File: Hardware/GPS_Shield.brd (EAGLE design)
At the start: 59.7 x 53.3 mm, 52 parts, among them J1 ARDUINO_R3_SHIELD, J2 USD_CONNECTOR, U1 APK2112-3.3V, U2 GP3906-TLP, U3 TXB0108

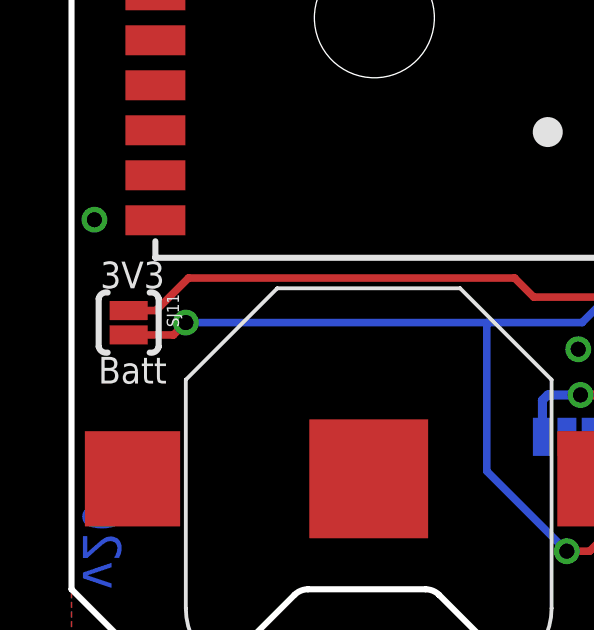
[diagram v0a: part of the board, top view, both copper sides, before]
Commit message: Default SJ11 to open.
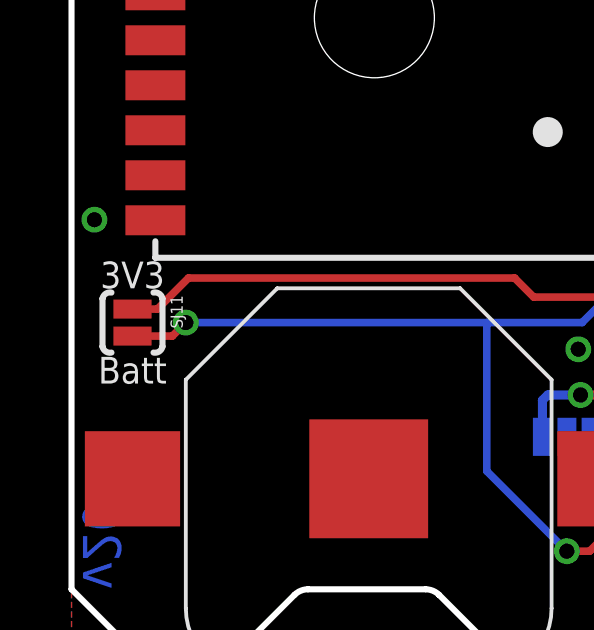
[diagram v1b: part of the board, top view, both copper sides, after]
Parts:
- SJ11: device SparkFun-Passives:PAD-JUMPER-2-NC_BY_PASTE_YES_SILK -> SparkFun-Passives:PAD-JUMPER-2-NO_YES_SILK
- moved SJ11 0.13 mm to (2.03, 11.4)
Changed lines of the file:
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@@
 <layer number="29" name="tStop" color="7" fill="3" visible="no" active="yes"/>
 <layer number="30" name="bStop" color="7" fill="6" visible="no" active="yes"/>
-<layer number="31" name="tCream" color="7" fill="4" visible="no" active="yes"/>
+<layer number="31" name="tCream" color="7" fill="4" visible="yes" active="yes"/>
 <layer number="32" name="bCream" color="7" fill="5" visible="no" active="yes"/>
 <layer number="33" name="tFinish" color="6" fill="3" visible="no" active="yes"/>
@@
 <attribute name="PROD_ID" value="CONN-08438" x="21.59" y="15.24" size="1.778" layer="27" font="vector" ratio="15" rot="R90" display="off"/>
 </element>
-<element name="SJ11" library="SparkFun-Passives" package="PAD-JUMPER-2-NC_BY_PASTE_YES_SILK" value="VBAT-3.3V" x="1.905" y="11.43" rot="R270"/>
+<element name="SJ11" library="SparkFun-Passives" package="PAD-JUMPER-2-NO_YES_SILK" value="VBAT-3.3V" x="2.032" y="11.43" rot="R270"/>
 </elements>
 <signals>
@@
 <wire x1="21.59" y1="5.08" x2="19.812" y2="6.858" width="0.3048" layer="16"/>
 <wire x1="17.995" y1="35.98" x2="19.265" y2="34.71" width="0.2032" layer="1"/>
-<contactref element="SJ11" pad="1"/>
 <wire x1="19.05" y1="12.28" x2="15.406" y2="12.28" width="0.254" layer="1"/>
 <wire x1="15.406" y1="12.28" x2="14.771" y2="12.915" width="0.254" layer="1"/>
-<wire x1="1.905" y1="11.8309" x2="2.8139" y2="11.8309" width="0.254" layer="1"/>
-<wire x1="2.8139" y1="11.8309" x2="3.898" y2="12.915" width="0.254" layer="1"/>
 <wire x1="3.898" y1="12.915" x2="14.771" y2="12.915" width="0.254" layer="1"/>
 <wire x1="19.812" y1="6.858" x2="19.812" y2="7.62" width="0.3048" layer="16"/>
@@
 <wire x1="19.812" y1="13.462" x2="21.59" y2="15.24" width="0.3048" layer="16"/>
 <wire x1="17.3228" y1="7.62" x2="19.812" y2="7.62" width="0.3048" layer="16"/>
+<contactref element="SJ11" pad="1"/>
+<wire x1="2.032" y1="11.88" x2="2.863" y2="11.88" width="0.254" layer="1"/>
+<wire x1="2.863" y1="11.88" x2="3.898" y2="12.915" width="0.254" layer="1"/>
 </signal>
 <signal name="5V">
@@
 <wire x1="21.59" y1="17.78" x2="19.05" y2="15.24" width="0.254" layer="16"/>
 <wire x1="19.05" y1="15.24" x2="19.05" y2="13.462" width="0.254" layer="16"/>
+<wire x1="3.36" y1="10.98" x2="3.81" y2="11.43" width="0.254" layer="1"/>
+<via x="3.81" y="11.43" extent="1-16" drill="0.508"/>
 <contactref element="SJ11" pad="2"/>
-<wire x1="1.905" y1="11.0173" x2="3.3973" y2="11.0173" width="0.254" layer="1"/>
-<wire x1="3.3973" y1="11.0173" x2="3.81" y2="11.43" width="0.254" layer="1"/>
-<via x="3.81" y="11.43" extent="1-16" drill="0.508"/>
+<wire x1="2.032" y1="10.98" x2="3.36" y2="10.98" width="0.254" layer="1"/>
 </signal>
 <signal name="CD">

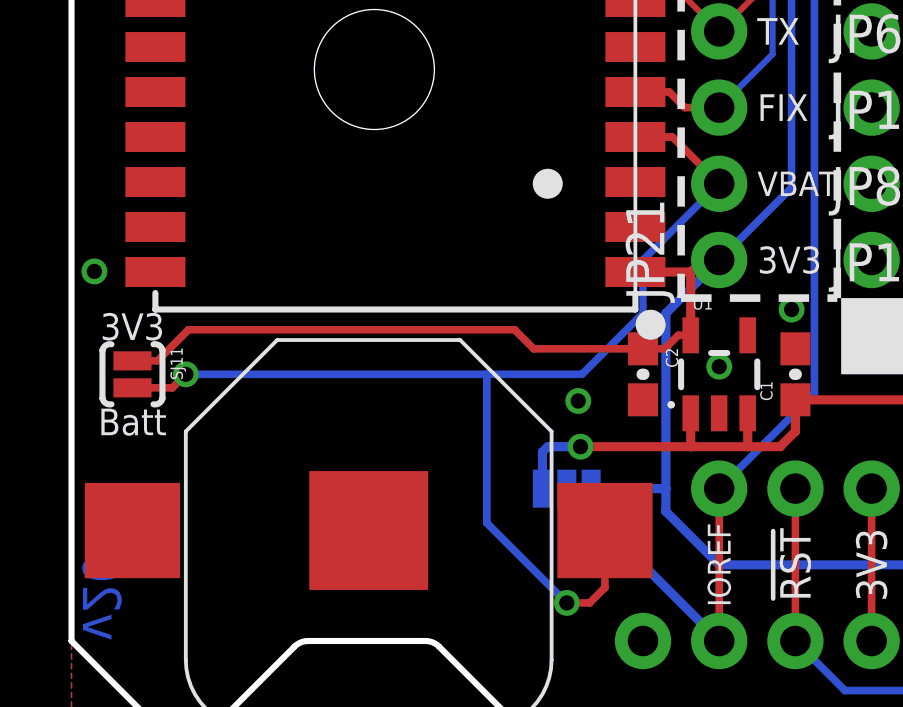
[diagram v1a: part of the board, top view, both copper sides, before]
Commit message: Adding note about battery required.
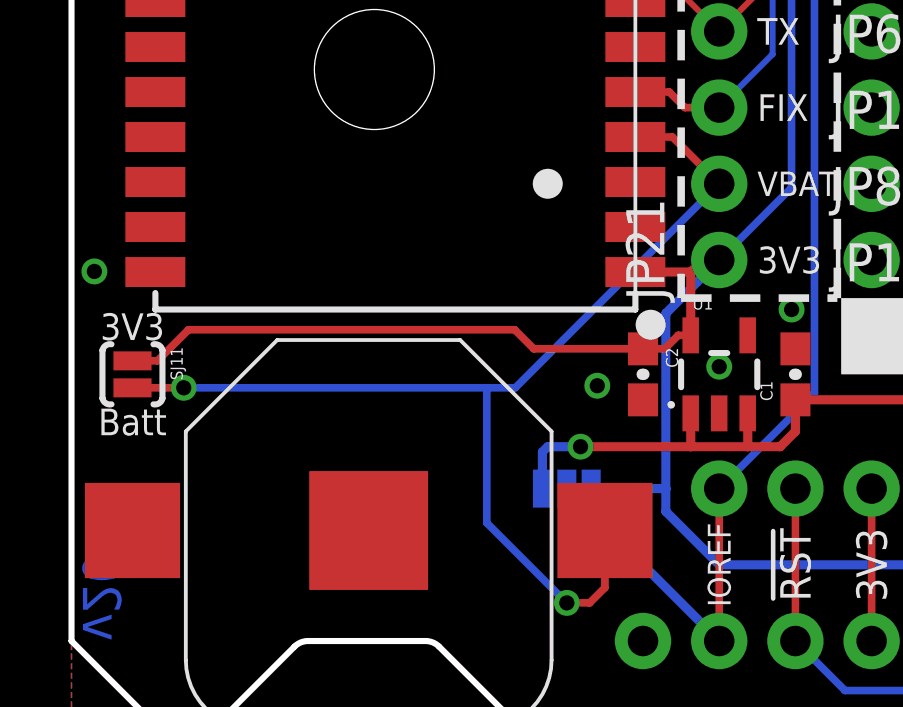
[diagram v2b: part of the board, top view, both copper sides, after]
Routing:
- net V_BATT: track 39.0 -> 37.5 mm
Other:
- board text added: "Battery supply required for operation!"
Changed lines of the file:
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@@
 <setting verticaltext="up"/>
 </settings>
-<grid distance="0.05" unitdist="inch" unit="inch" style="lines" multiple="1" display="yes" altdistance="0.0025" altunitdist="inch" altunit="inch"/>
+<grid distance="0.05" unitdist="inch" unit="inch" style="lines" multiple="1" display="yes" altdistance="0.005" altunitdist="inch" altunit="inch"/>
 <layers>
 <layer number="1" name="Top" color="4" fill="1" visible="yes" active="yes"/>
@@
 <layer number="29" name="tStop" color="7" fill="3" visible="no" active="yes"/>
 <layer number="30" name="bStop" color="7" fill="6" visible="no" active="yes"/>
-<layer number="31" name="tCream" color="7" fill="4" visible="yes" active="yes"/>
+<layer number="31" name="tCream" color="7" fill="4" visible="no" active="yes"/>
 <layer number="32" name="bCream" color="7" fill="5" visible="no" active="yes"/>
 <layer number="33" name="tFinish" color="6" fill="3" visible="no" active="yes"/>
@@
 <text x="53.6575" y="30.48" size="0.8128" layer="22" font="vector" ratio="15" rot="MR0" align="center-left">MISO</text>
 <text x="58.42" y="28.0035" size="0.8128" layer="22" font="vector" ratio="15" rot="MR270" align="top-center">MOSI</text>
+<text x="12.573" y="7.366" size="1.016" layer="22" font="vector" ratio="15" rot="MR0" align="top-left">Battery supply
+required for
+operation!</text>
 </plain>
 <attributes>
@@
 <via x="19.05" y="37.084" extent="1-16" drill="0.508"/>
 <via x="21.59" y="11.684" extent="1-16" drill="0.508"/>
-<via x="16.891" y="10.541" extent="1-16" drill="0.508"/>
+<via x="17.526" y="11.049" extent="1-16" drill="0.508"/>
 <via x="24.003" y="13.589" extent="1-16" drill="0.508"/>
 <via x="0.762" y="14.859" extent="1-16" drill="0.508"/>
@@
 <contactref element="BAT1" pad="PWR@1"/>
 <contactref element="U2" pad="4"/>
-<wire x1="3.81" y1="11.43" x2="13.843" y2="11.43" width="0.254" layer="16"/>
-<wire x1="13.843" y1="11.43" x2="17.018" y2="11.43" width="0.254" layer="16"/>
-<wire x1="19.05" y1="13.462" x2="17.018" y2="11.43" width="0.254" layer="16"/>
-<wire x1="13.843" y1="11.43" x2="13.843" y2="6.477" width="0.254" layer="16"/>
 <wire x1="13.843" y1="6.477" x2="16.51" y2="3.81" width="0.254" layer="16"/>
 <via x="16.51" y="3.81" extent="1-16" drill="0.508"/>
@@
 <wire x1="18.795" y1="19.34" x2="20.03" y2="19.34" width="0.254" layer="1"/>
 <wire x1="20.03" y1="19.34" x2="21.59" y2="17.78" width="0.254" layer="1"/>
-<wire x1="21.59" y1="17.78" x2="19.05" y2="15.24" width="0.254" layer="16"/>
-<wire x1="19.05" y1="15.24" x2="19.05" y2="13.462" width="0.254" layer="16"/>
-<wire x1="3.36" y1="10.98" x2="3.81" y2="11.43" width="0.254" layer="1"/>
-<via x="3.81" y="11.43" extent="1-16" drill="0.508"/>
 <contactref element="SJ11" pad="2"/>
-<wire x1="2.032" y1="10.98" x2="3.36" y2="10.98" width="0.254" layer="1"/>
+<wire x1="2.032" y1="10.98" x2="3.741" y2="10.98" width="0.254" layer="1"/>
+<wire x1="14.79" y1="10.98" x2="21.59" y2="17.78" width="0.254" layer="16"/>
+<via x="3.741" y="10.98" extent="1-16" drill="0.508"/>
+<wire x1="3.741" y1="10.98" x2="13.843" y2="10.98" width="0.254" layer="16"/>
+<wire x1="13.843" y1="10.98" x2="14.79" y2="10.98" width="0.254" layer="16"/>
+<wire x1="13.843" y1="6.477" x2="13.843" y2="10.98" width="0.254" layer="16"/>
 </signal>
 <signal name="CD">

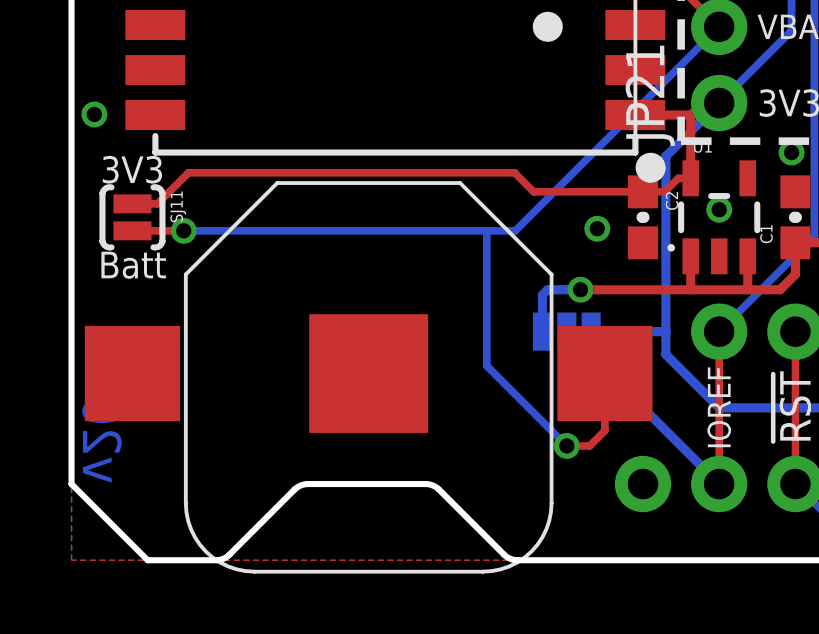
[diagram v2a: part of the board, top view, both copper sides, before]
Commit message: Updating 12mm battery PROD_ID
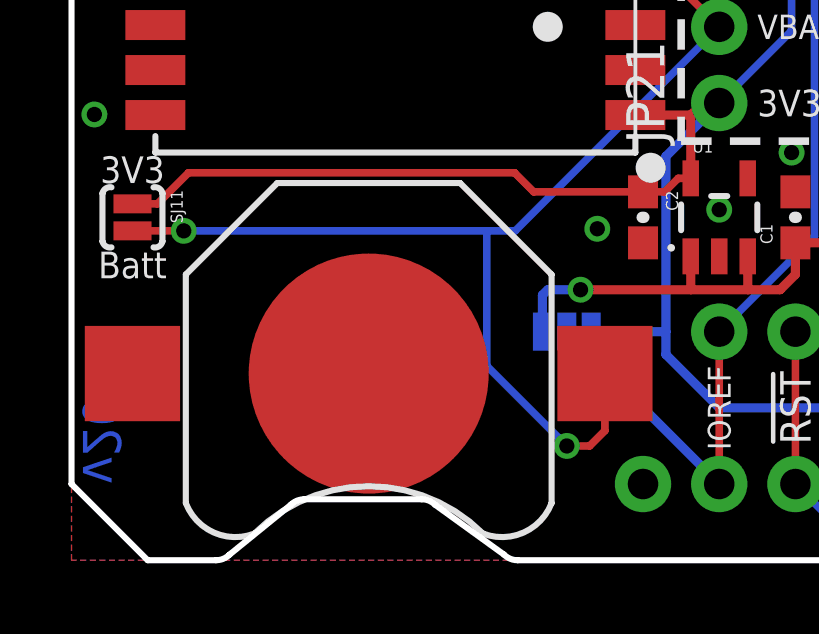
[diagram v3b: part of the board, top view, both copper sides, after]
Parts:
- BAT1: device SparkFun:BATTCON_12MM -> SparkFun-Electromechanical:BATTCON_12MM
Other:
- outline, holes or cut-outs redrawn
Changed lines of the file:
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@@
 <wire x1="57.15" y1="0" x2="14.868025" y2="0" width="0.2032" layer="20"/>
 <wire x1="14.868025" y1="0" x2="14.4190125" y2="0.1859875" width="0.2032" layer="20" curve="-45"/>
-<wire x1="14.4190125" y1="0.1859875" x2="12.2509875" y2="2.3540125" width="0.2032" layer="20"/>
-<wire x1="12.2509875" y1="2.3540125" x2="11.801975" y2="2.54" width="0.2032" layer="20" curve="45"/>
-<wire x1="11.801975" y1="2.54" x2="7.883025" y2="2.54" width="0.2032" layer="20"/>
-<wire x1="7.883025" y1="2.54" x2="7.4340125" y2="2.3540125" width="0.2032" layer="20" curve="45"/>
-<wire x1="7.4340125" y1="2.3540125" x2="5.2659875" y2="0.1859875" width="0.2032" layer="20"/>
+<wire x1="14.4190125" y1="0.1859875" x2="12.1239875" y2="1.8460125" width="0.2032" layer="20"/>
+<wire x1="12.1239875" y1="1.8460125" x2="11.674975" y2="2.032" width="0.2032" layer="20" curve="45"/>
+<wire x1="11.674975" y1="2.032" x2="7.756025" y2="2.032" width="0.2032" layer="20"/>
+<wire x1="7.756025" y1="2.032" x2="7.3070125" y2="1.8460125" width="0.2032" layer="20" curve="45"/>
+<wire x1="7.3070125" y1="1.8460125" x2="5.2659875" y2="0.1859875" width="0.2032" layer="20"/>
 <wire x1="5.2659875" y1="0.1859875" x2="4.816975" y2="0" width="0.2032" layer="20" curve="-45"/>
 <wire x1="4.816975" y1="0" x2="2.54" y2="0" width="0.2032" layer="20"/>
@@
 </autorouter>
 <elements>
-<element name="BAT1" library="SparkFun" package="BATTCON_12MM" value="12mm" x="9.906" y="6.223" smashed="yes" rot="R180"/>
+<element name="BAT1" library="SparkFun-Electromechanical" package="BATTCON_12MM" value="12mm" x="9.906" y="6.223" smashed="yes" rot="R180">
+<attribute name="PROD_ID" value="BATT-08044" x="9.906" y="6.223" size="1.778" layer="27" rot="R180" display="off"/>
+</element>
 <element name="C3" library="SparkFun-Capacitors" package="0603-CAP" value="0.1uF" x="27.305" y="39.37" smashed="yes" rot="R270">
 <attribute name="NAME" x="28.0035" y="40.259" size="0.4064" layer="25" rot="R270"/>
